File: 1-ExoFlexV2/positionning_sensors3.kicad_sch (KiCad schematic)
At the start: 41 parts, among them U60 ADCMP602BRMZ, U61 ADCMP602BRMZ, U62 ADCMP602BRMZ, U63 SN74LVC1G08DBVR, U64 SN74LVC1G08DBVR, U65 SN74LVC3G14DCUT_V2

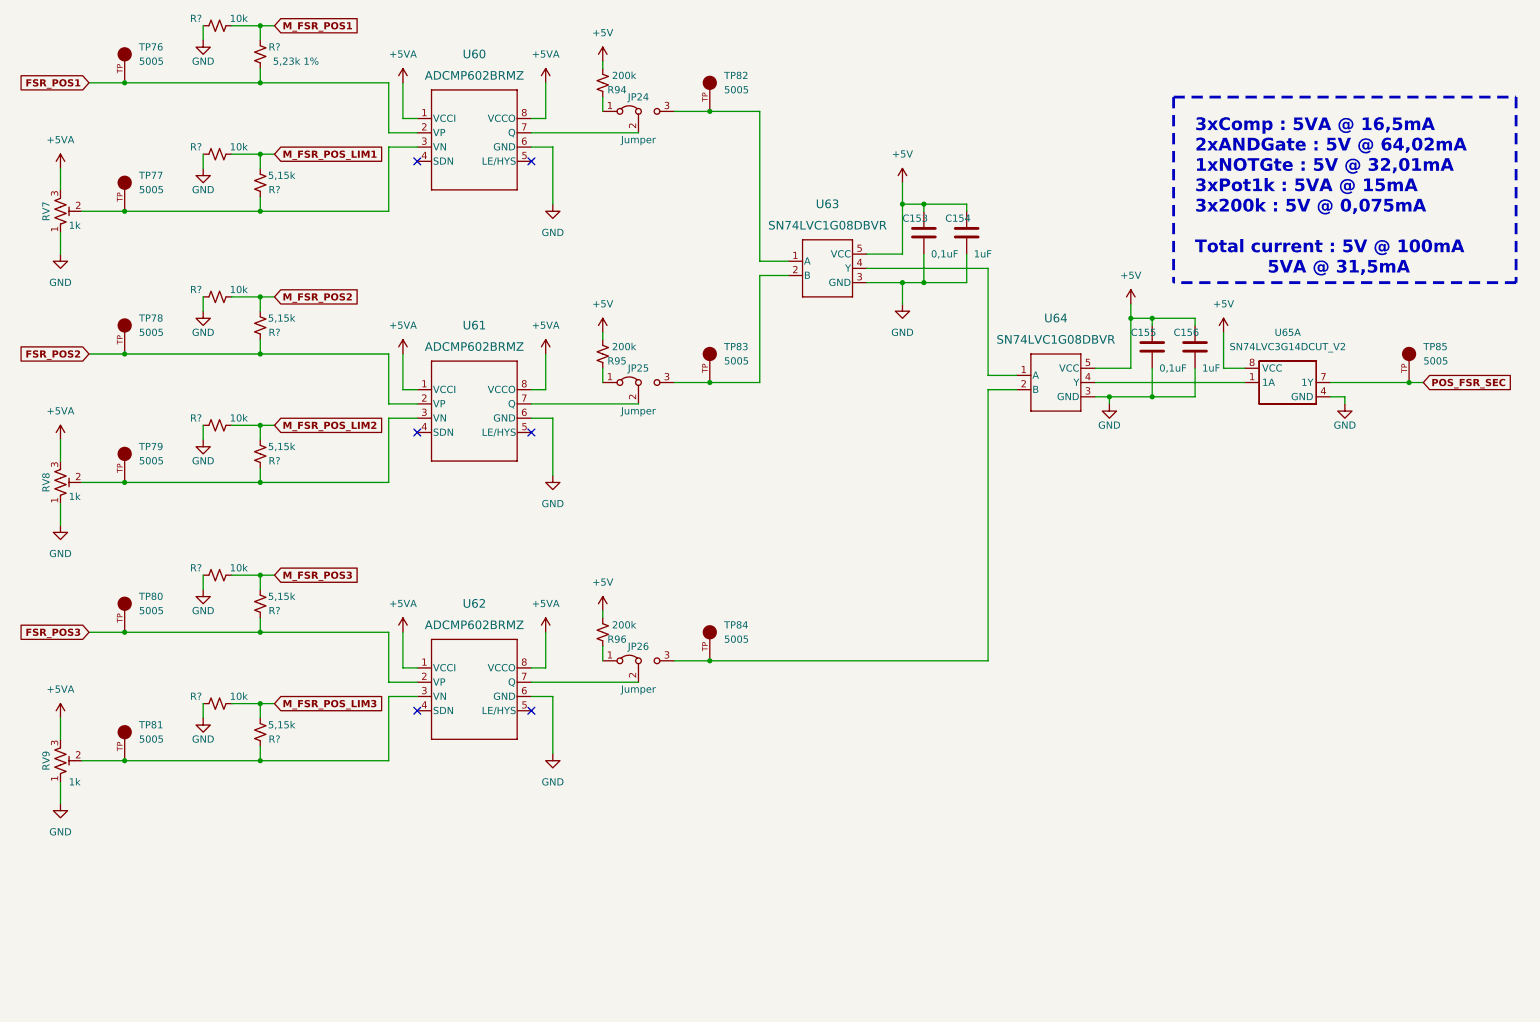
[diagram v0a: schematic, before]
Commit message: Finalisation 2
-Ajout des nouveaux comparateurs
- Ajout d'une page découplage
- Retrait des condensateur dans les autres pages
- Ajout de trimmer pour les résistance importante mais incertaines
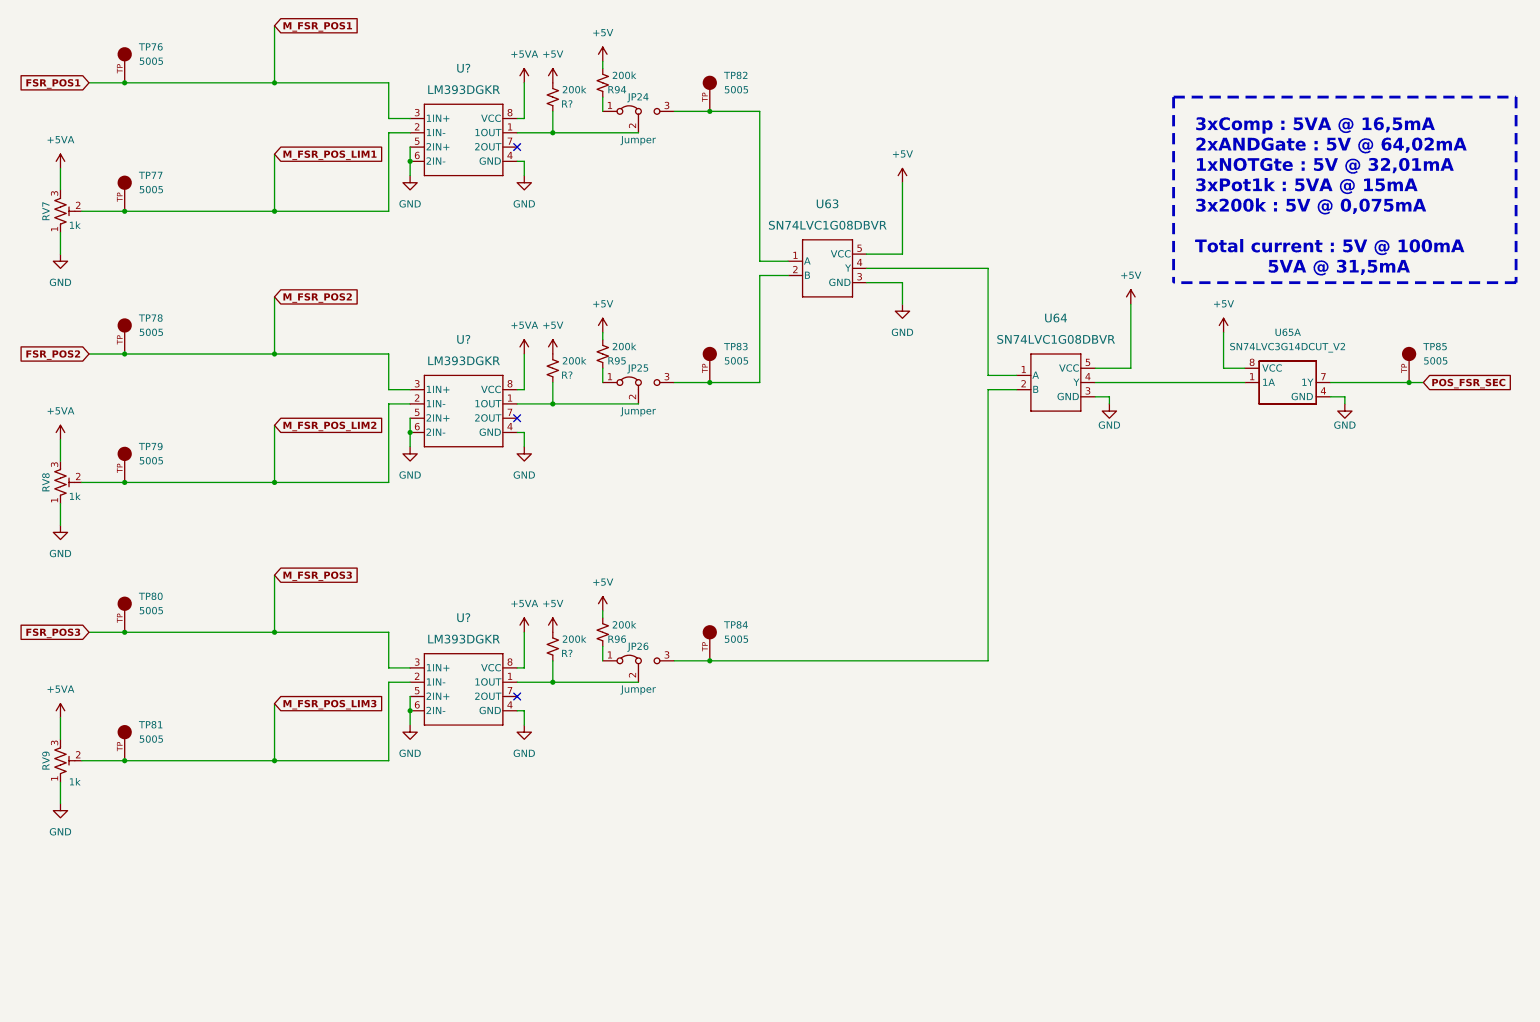
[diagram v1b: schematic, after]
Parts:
- removed C153, C155: 0,1uF, Capacitor_SMD:C_0603_1608Metric, symbol Device:C
- removed C154, C156: 1uF, Capacitor_SMD:C_0603_1608Metric, symbol Device:C
- removed R? (x5): 5,15k, Resistor_SMD:R_0805_2012Metric, symbol Device:R_Small_US
- removed R? (x6): 10k, Resistor_SMD:R_0805_2012Metric, symbol Device:R_Small_US
- removed R?: 5,23k 1%, Resistor_SMD:R_0805_2012Metric, symbol Device:R_Small_US
- removed U60, U61, U62: ADCMP602BRMZ, FootPrint:ADCMP602BRMZ, symbol SymLib:ADCMP602BRMZ
- added R? (x3): 200k, Resistor_SMD:R_0603_1608Metric, symbol Device:R_Small_US
- added U? (x3): LM393DGKR, DGK8, symbol SymLib:LM393DGKR
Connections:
- net +5V: now also R?.1, R?.1, R?.1
- net +5VA: now also U?.8 (VCC), U?.8 (VCC), U?.8 (VCC)
- net FSR_POS1: now also U?.3 (1IN+)
- net FSR_POS2: now also U?.3 (1IN+)
- net FSR_POS3: now also U?.3 (1IN+)
- net GND: now also U?.4 (GND), U?.4 (GND), U?.4 (GND), U?.5 (2IN+), U?.5 (2IN+), U?.5 (2IN+), U?.6 (2IN-), U?.6 (2IN-), U?.6 (2IN-)
- net M_FSR_POS_LIM1: now also RV7.2, TP77.TP, U?.2 (1IN-)
- net M_FSR_POS_LIM2: now also RV8.2, TP79.TP, U?.2 (1IN-)
- net M_FSR_POS_LIM3: now also RV9.2, TP81.TP, U?.2 (1IN-)
- net at JP26.2 (C): now also R?.2, U?.1 (1OUT)
- net at JP25.2 (C): now also R?.2, U?.1 (1OUT)
- net at JP24.2 (C): now also R?.2, U?.1 (1OUT)
- no-connect marks 6 -> 3

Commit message: Chokes et RC
- Ajout des RF chokes
- Changement des résistance pour 0805
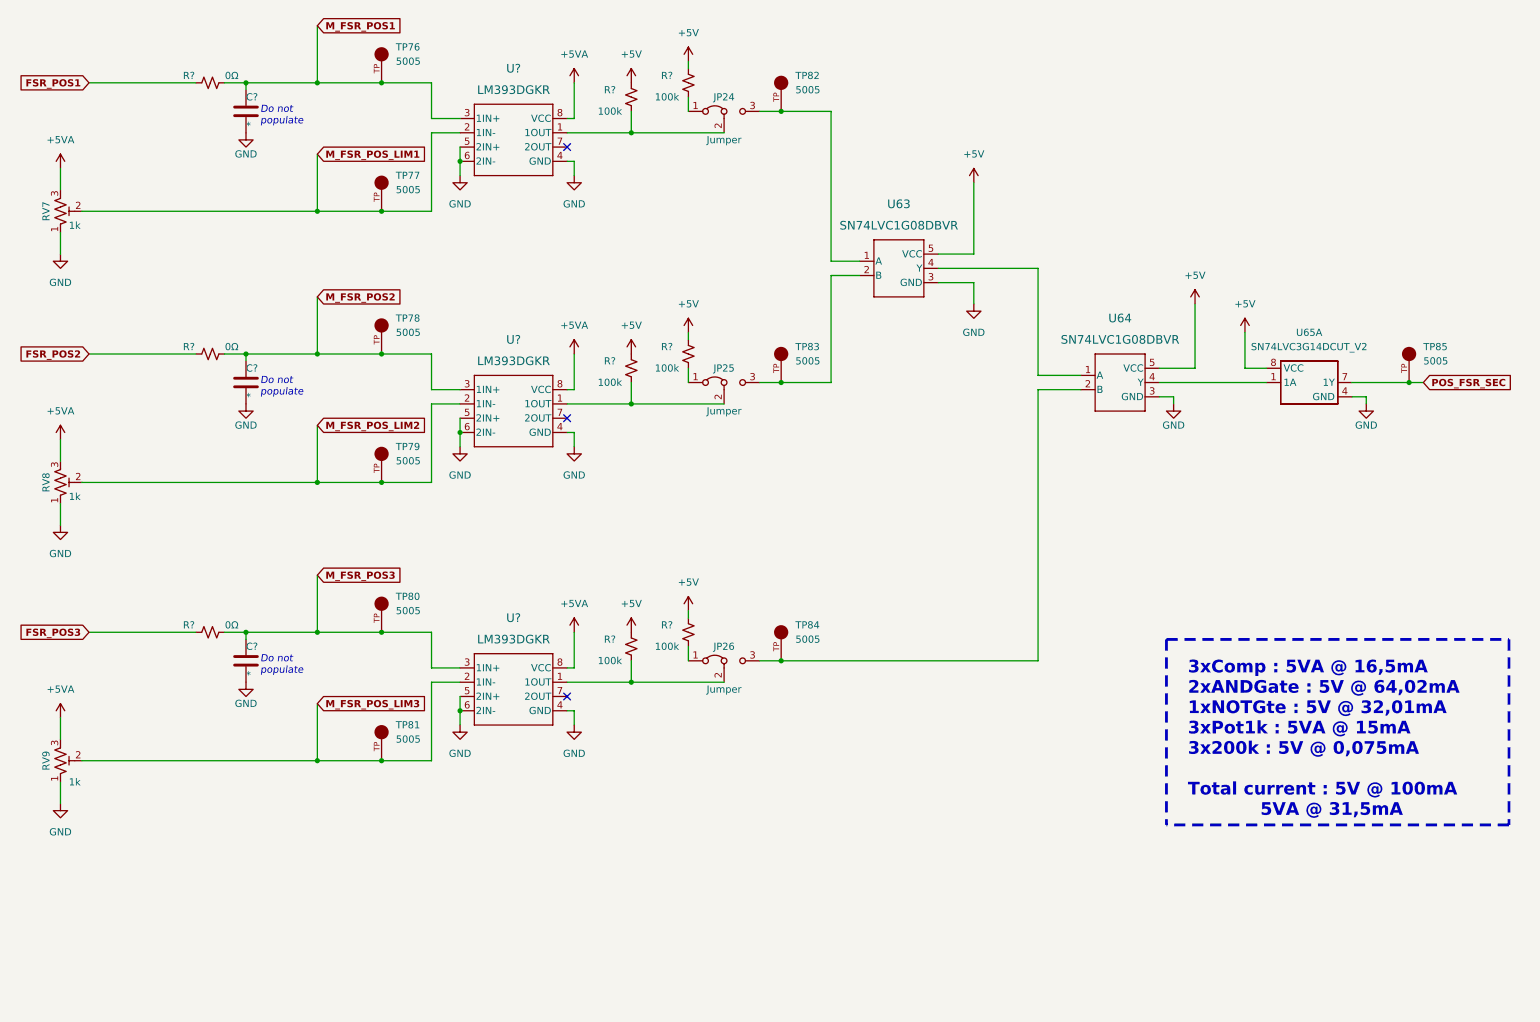
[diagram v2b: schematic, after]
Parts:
- removed R94, R95, R96, R? (x3): 200k, Resistor_SMD:R_0603_1608Metric, symbol Device:R_Small_US
- added C? (x3): *, Capacitor_SMD:C_0805_2012Metric, symbol Device:C
- added R? (x3): 0Ω, Resistor_SMD:R_0805_2012Metric, symbol Device:R_Small_US
- added R? (x6): 100k, Resistor_SMD:R_0805_2012Metric, symbol Device:R_Small_US
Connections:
- net +5V: now also R?.1, R?.1, R?.1, R?.1, R?.1, R?.1
- net FSR_POS1: now also R?.1; no longer TP76.TP, U?.3 (1IN+)
- net FSR_POS2: now also R?.1; no longer TP78.TP, U?.3 (1IN+)
- net FSR_POS3: now also R?.1; no longer TP80.TP, U?.3 (1IN+)
- net GND: now also C?.2, C?.2, C?.2
- net at JP25.1 (A): now also R?.2
- net at JP25.2 (C), U?.1 (1OUT): now also R?.2
- net at JP26.2 (C), U?.1 (1OUT): now also R?.2
- net at JP26.1 (A): now also R?.2
- net at JP24.1 (A): now also R?.2
- net at JP24.2 (C), U?.1 (1OUT): now also R?.2
- new net M_FSR_POS1: C?.1, R?.2, TP76.TP, U?.3 (1IN+)
- new net M_FSR_POS2: C?.1, R?.2, TP78.TP, U?.3 (1IN+)
- new net M_FSR_POS3: C?.1, R?.2, TP80.TP, U?.3 (1IN+)
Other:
- note added: "Do not populate"
- moved on the sheet: JP24, JP25, JP26, TP76, TP77, TP78, TP79, TP80, TP81, TP82, TP83, TP84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

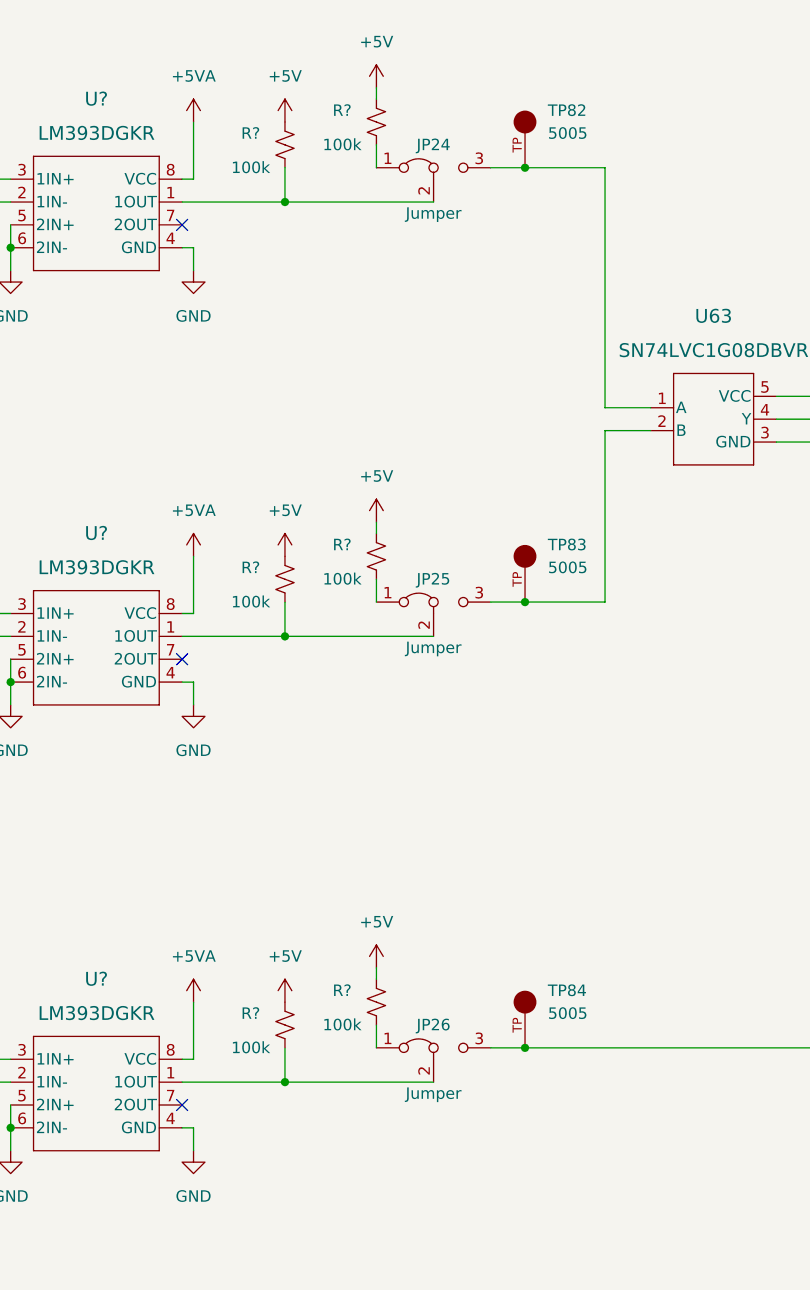
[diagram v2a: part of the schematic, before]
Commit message: Trimmer et jumper
-Changement de symbole de jumper
-Ajout des des trimmer aux endroits nécessaires
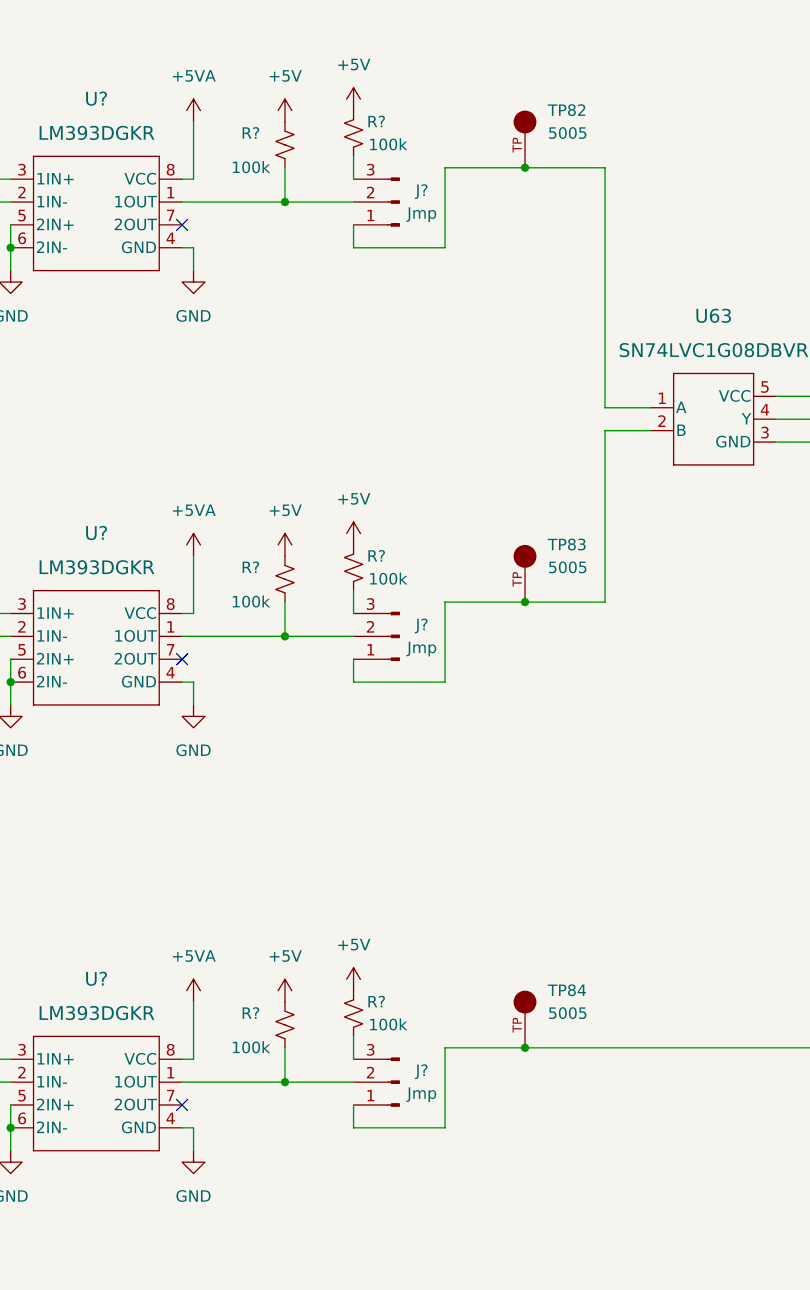
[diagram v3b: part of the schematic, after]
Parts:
- removed JP24, JP25, JP26: Jumper, Connector_PinHeader_2.54mm:PinHeader_1x03_P2.54mm_Vertical, symbol Jumper:Jumper_3_Bridged12
- removed R? (x3): 100k, Resistor_SMD:R_0805_2012Metric, symbol Device:R_Small_US
- added J? (x3): Jmp, symbol Connector:Conn_01x03_Male
- added R? (x3): 100k, Resistor_SMD:R_0805_2012Metric, symbol Device:R_Small_US
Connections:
- net +5V: now also R?.2, R?.2, R?.2
- net at TP82.TP, U63.1 (A): now also J?.1 (Pin_1)
- net at R?.2, U?.1 (1OUT): now also J?.2 (Pin_2) (x3)
- net at TP84.TP, U64.2 (B): now also J?.1 (Pin_1)
- net at TP83.TP, U63.2 (B): now also J?.1 (Pin_1)
- new net: J?.3 (Pin_3), R?.1 (x3)
